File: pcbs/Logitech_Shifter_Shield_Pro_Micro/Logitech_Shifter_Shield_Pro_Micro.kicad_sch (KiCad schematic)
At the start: 12 parts, among them J1 DE9_Plug_MountingHoles, J2 AVR-ISP-6, U1 SparkFun_ProMicro

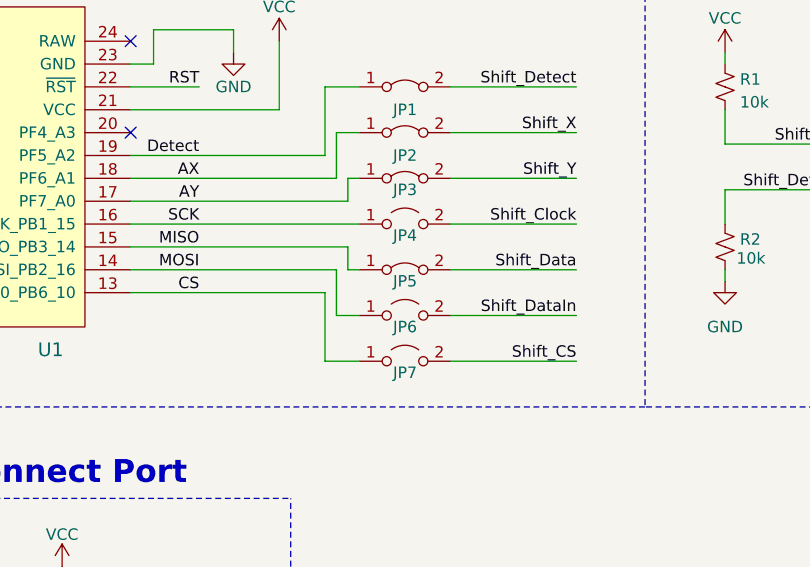
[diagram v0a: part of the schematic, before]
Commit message: Shifter: Changed all jumpers to NC
We need all of these pins in order to interface with the Logitech G25 shifter
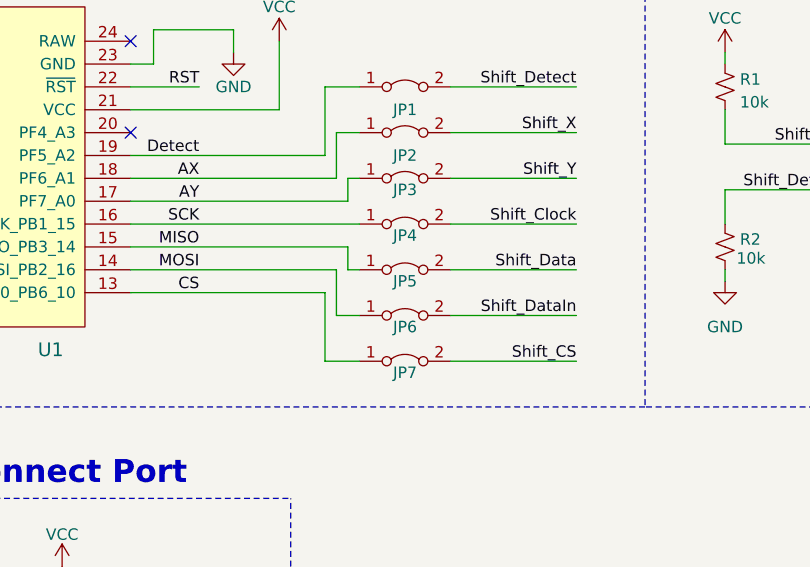
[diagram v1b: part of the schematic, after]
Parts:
- removed JP4: Clock_Jumper_NC, Jumper:SolderJumper-2_P1.3mm_Open_RoundedPad1.0x1.5mm, symbol Jumper:Jumper_2_Open
- removed JP6: Data_In_Jumper_NC, Jumper:SolderJumper-2_P1.3mm_Open_RoundedPad1.0x1.5mm, symbol Jumper:Jumper_2_Open
- removed JP7: CS_Jumper_NC, Jumper:SolderJumper-2_P1.3mm_Open_RoundedPad1.0x1.5mm, symbol Jumper:Jumper_2_Open
- added JP4: Clock_Jumper, Sim_Racing_Shields:SolderJumper-2_P1.3mm_Bridged_RoundedPad1.0x1.5mm_Unmasked, symbol Jumper:Jumper_2_Bridged
- added JP6: Data_In_Jumper, Sim_Racing_Shields:SolderJumper-2_P1.3mm_Bridged_RoundedPad1.0x1.5mm_Unmasked, symbol Jumper:Jumper_2_Bridged
- added JP7: CS_Jumper, Sim_Racing_Shields:SolderJumper-2_P1.3mm_Bridged_RoundedPad1.0x1.5mm_Unmasked, symbol Jumper:Jumper_2_Bridged
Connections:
- net CS: now also JP7.1 (A)
- net MOSI: now also JP6.1 (A)
- net SCK: now also JP4.1 (A)
- net Shift_CS: now also JP7.2 (B)
- net Shift_Clock: now also JP4.2 (B)
- net Shift_DataIn: now also JP6.2 (B)
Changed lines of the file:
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@@
+	)
+	(symbol
+		(lib_id "Jumper:Jumper_2_Bridged")
+		(at 144.78 96.52 0)
+		(unit 1)
+		(exclude_from_sim no)
+		(in_bom no)
+		(on_board yes)
+		(dnp no)
+		(property "Reference" "JP7"
+			(at 144.78 97.79 0)
+			(effects
+				(font
+					(size 1.27 1.27)
+				)
+			)
+		)
+		(property "Value" "CS_Jumper"
+			(at 144.78 94.6936 0)
+			(effects
+				(font
+					(size 1.27 1.27)
+				)
+				(hide yes)
+			)
+		)
+		(property "Footprint" "Sim_Racing_Shields:SolderJumper-2_P1.3mm_Bridged_RoundedPad1.0x1.5mm_Unmasked"
+			(at 144.78 96.52 0)
+			(effects
+				(font
+					(size 1.27 1.27)
+				)
+				(hide yes)
+			)
+		)
+		(property "Datasheet" "~"
+			(at 144.78 96.52 0)
+			(effects
+				(font
+					(size 1.27 1.27)
+				)
+				(hide yes)
+			)
+		)
+		(property "Description" ""
+			(at 144.78 96.52 0)
+			(effects
+				(font
+					(size 1.27 1.27)
+				)
+				(hide yes)
+			)
+		)
+		(property "DigiKey Part Number" ""
+			(at 144.78 96.52 0)
+			(effects
+				(font
+					(size 1.27 1.27)
+				)
+				(hide yes)
+			)
+		)
+		(property "Manufacturer" ""
+			(at 144.78 96.52 0)
+			(effects
+				(font
+					(size 1.27 1.27)
+				)
+				(hide yes)
+			)
+		)
+		(property "Part Number" ""
+			(at 144.78 96.52 0)
+			(effects
+				(font
+					(size 1.27 1.27)
+				)
+				(hide yes)
+			)
+		)
+		(pin "1"
+		)
+		(pin "2"
+		)
+		(instances
+			(project "Logitech_Shifter_Shield_Pro_Micro"
+				(path "/e63e39d7-6ac0-4ffd-8aa3-1841a4541b55"
+					(reference "JP7")
+					(unit 1)
+				)
+			)
+		)
 	)
 	(symbol
@@
 	)
 	(symbol
+		(lib_id "Jumper:Jumper_2_Bridged")
+		(at 144.78 81.28 0)
+		(unit 1)
+		(exclude_from_sim no)
+		(in_bom no)
+		(on_board yes)
+		(dnp no)
+		(property "Reference" "JP4"
+			(at 144.78 82.55 0)
+			(effects
+				(font
+					(size 1.27 1.27)
+				)
+			)
+		)
+		(property "Value" "Clock_Jumper"
+			(at 144.78 79.4536 0)
+			(effects
+				(font
+					(size 1.27 1.27)
+				)
+				(hide yes)
+			)
+		)
+		(property "Footprint" "Sim_Racing_Shields:SolderJumper-2_P1.3mm_Bridged_RoundedPad1.0x1.5mm_Unmasked"
+			(at 144.78 81.28 0)
+			(effects
+				(font
+					(size 1.27 1.27)
+				)
+				(hide yes)
+			)
+		)
+		(property "Datasheet" "~"
+			(at 144.78 81.28 0)
+			(effects
+				(font
+					(size 1.27 1.27)
+				)
+				(hide yes)
+			)
+		)
+		(property "Description" ""
+			(at 144.78 81.28 0)
+			(effects
+				(font
+					(size 1.27 1.27)
+				)
+				(hide yes)
+			)
+		)
+		(property "DigiKey Part Number" ""
+			(at 144.78 81.28 0)
+			(effects
+				(font
+					(size 1.27 1.27)
+				)
+				(hide yes)
+			)
+		)
+		(property "Manufacturer" ""
+			(at 144.78 81.28 0)
+			(effects
+				(font
+					(size 1.27 1.27)
+				)
+				(hide yes)
+			)
+		)
+		(property "Part Number" ""
+			(at 144.78 81.28 0)
+			(effects
+				(font
+					(size 1.27 1.27)
+				)
+				(hide yes)
+			)
+		)
+		(pin "1"
+		)
+		(pin "2"
+		)
+		(instances
+			(project "Logitech_Shifter_Shield_Pro_Micro"
+				(path "/e63e39d7-6ac0-4ffd-8aa3-1841a4541b55"
+					(reference "JP4")
+					(unit 1)
+				)
+			)
+		)
+	)
+	(symbol
 		(lib_id "Sim_Racing_Shields:SparkFun_ProMicro")
 		(at 93.98 80.01 0)
@@
 				(path "/e63e39d7-6ac0-4ffd-8aa3-1841a4541b55"
 					(reference "U1")
-					(unit 1)
-				)
-			)
-		)
-	)
-	(symbol
-		(lib_id "Jumper:Jumper_2_Open")
-		(at 144.78 96.52 0)
-		(unit 1)
-		(exclude_from_sim no)
-		(in_bom no)
-		(on_board yes)
-		(dnp no)
-		(property "Reference" "JP7"
-			(at 144.78 97.79 0)
-			(effects
-				(font
-					(size 1.27 1.27)
-				)
-			)
-		)
-		(property "Value" "CS_Jumper_NC"
-			(at 144.78 93.345 0)
-			(effects
-				(font
-					(size 1.27 1.27)
-				)
-				(hide yes)
-			)
-		)
-		(property "Footprint" "Jumper:SolderJumper-2_P1.3mm_Open_RoundedPad1.0x1.5mm"
-			(at 144.78 96.52 0)
-			(effects
-				(font
-					(size 1.27 1.27)
-				)
-				(hide yes)
-			)
-		)
-		(property "Datasheet" "~"
-			(at 144.78 96.52 0)
-			(effects
-				(font
-					(size 1.27 1.27)
-				)
-				(hide yes)
-			)
-		)
-		(property "Description" ""
-			(at 144.78 96.52 0)
-			(effects
-				(font
-					(size 1.27 1.27)
-				)
-				(hide yes)
-			)
-		)
-		(property "DigiKey Part Number" ""
-			(at 144.78 96.52 0)
-			(effects
-				(font
-					(size 1.27 1.27)
-				)
-				(hide yes)
-			)
-		)
-		(property "Manufacturer" ""
-			(at 144.78 96.52 0)
-			(effects
-				(font
-					(size 1.27 1.27)
-				)
-				(hide yes)
-			)
-		)
-		(property "Part Number" ""
-			(at 144.78 96.52 0)
-			(effects
-				(font
-					(size 1.27 1.27)
-				)
-				(hide yes)
-			)
-		)
-		(pin "1"
-		)
-		(pin "2"
-		)
-		(instances
-			(project ""
-				(path "/e63e39d7-6ac0-4ffd-8aa3-1841a4541b55"
-					(reference "JP7")
 					(unit 1)
 				)
@@
 	)
 	(symbol
-		(lib_id "Jumper:Jumper_2_Open")
+		(lib_id "Jumper:Jumper_2_Bridged")
 		(at 144.78 91.44 0)
 		(unit 1)
@@
 			)
 		)
-		(property "Value" "Data_In_Jumper_NC"
-			(at 144.78 88.265 0)
-			(effects
-				(font
-					(size 1.27 1.27)
-				)
-				(hide yes)
-			)
-		)
-		(property "Footprint" "Jumper:SolderJumper-2_P1.3mm_Open_RoundedPad1.0x1.5mm"
+		(property "Value" "Data_In_Jumper"
+			(at 144.78 89.6136 0)
+			(effects
+				(font
+					(size 1.27 1.27)
+				)
+				(hide yes)
+			)
+		)
+		(property "Footprint" "Sim_Racing_Shields:SolderJumper-2_P1.3mm_Bridged_RoundedPad1.0x1.5mm_Unmasked"
 			(at 144.78 91.44 0)
 			(effects
@@
 		)
 		(instances
-			(project ""
+			(project "Logitech_Shifter_Shield_Pro_Micro"
 				(path "/e63e39d7-6ac0-4ffd-8aa3-1841a4541b55"
 					(reference "JP6")
@@
 					(unit 1)
 				)
-			)
-		)
-	)
-	(symbol
-		(lib_id "Jumper:Jumper_2_Open")
-		(at 144.78 81.28 0)
-		(unit 1)
-		(exclude_from_sim no)
-		(in_bom no)
-		(on_board yes)
-		(dnp no)
-		(property "Reference" "JP4"
-			(at 144.78 82.55 0)
-			(effects
-				(font
-					(size 1.27 1.27)
-				)
-			)
-		)
-		(property "Value" "Clock_Jumper_NC"
-			(at 144.78 78.105 0)
-			(effects
-				(font
-					(size 1.27 1.27)
-				)
-				(hide yes)
-			)
-		)
-		(property "Footprint" "Jumper:SolderJumper-2_P1.3mm_Open_RoundedPad1.0x1.5mm"
-			(at 144.78 81.28 0)
-			(effects
-				(font
-					(size 1.27 1.27)
-				)
-				(hide yes)
-			)
-		)
-		(property "Datasheet" "~"
-			(at 144.78 81.28 0)
-			(effects
-				(font
-					(size 1.27 1.27)
-				)
-				(hide yes)
-			)
-		)
-		(property "Description" ""
-			(at 144.78 81.28 0)
-			(effects
-				(font
-					(size 1.27 1.27)
-				)
-				(hide yes)
-			)
-		)
-		(property "DigiKey Part Number" ""
-			(at 144.78 81.28 0)
-			(effects
-				(font
-					(size 1.27 1.27)
-				)
-				(hide yes)
-			)
-		)
-		(property "Manufacturer" ""
-			(at 144.78 81.28 0)
-			(effects
-				(font
-					(size 1.27 1.27)
-				)
-				(hide yes)
-			)
-		)
-		(property "Part Number" ""
-			(at 144.78 81.28 0)
-			(effects
-				(font
-					(size 1.27 1.27)
-				)
-				(hide yes)
-			)
-		)
-		(pin "1"
-		)
-		(pin "2"
-		)
-		(instances
-			(project ""
-				(path "/e63e39d7-6ac0-4ffd-8aa3-1841a4541b55"
-					(reference "JP4")
-					(unit 1)
-				)

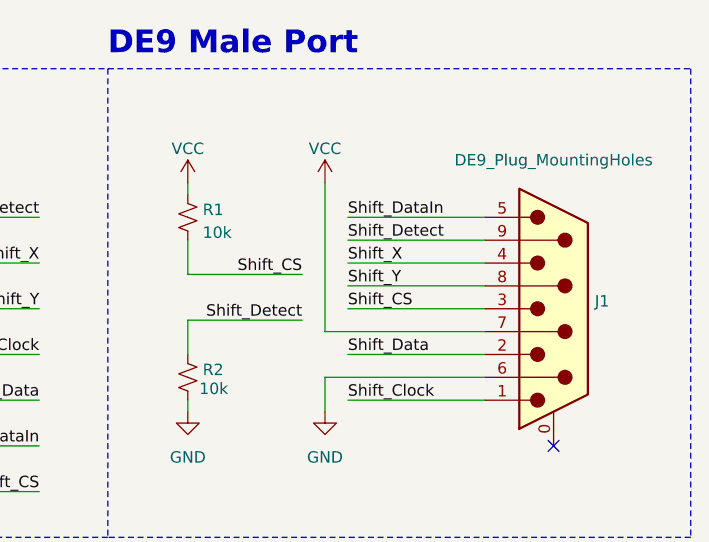
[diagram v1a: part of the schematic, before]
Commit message: Shifter: Move power to pin 9 (swap 7/9)
This is an error on the v1 PCB, and the fundamental reason why this PCB doesn't work with the G25 shifter.

On the Driving Force shifter, pins 7 and 9 are connected together internally in the DE-9 connector. Power applied to one goes to both pins, so one is used to power the shifter and the other is used with a pull-down to act as a detection pin. Since it didn't seem to matter I arbitrarily chose pin 7 as the power input for easier trace routing.

On the G25 shifter, pins *1* and 9 are connected together internally in the DE-9 connector. Pin 7 is instead attached to the clock input of the EEPROM / shift registers, and needs to be pulsed in order to get the button data from the shifter.

50/50 and I lost. Ah well.
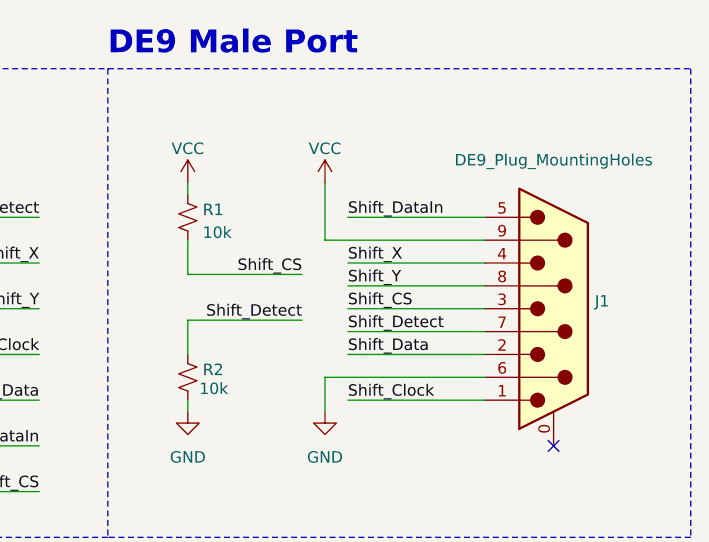
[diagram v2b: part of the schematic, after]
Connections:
- net Shift_Detect: now also J1.7; no longer J1.9
- net VCC: now also J1.9; no longer J1.7
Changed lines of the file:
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@@
 	(wire
 		(pts
-			(xy 195.58 78.74) (xy 213.36 78.74)
+			(xy 195.58 68.58) (xy 213.36 68.58)
+		)
+		(stroke
+			(width 0)
+			(type default)
+		)
+	)
+	(wire
+		(pts
+			(xy 198.12 78.74) (xy 213.36 78.74)
 		)
 		(stroke
@@
 	(wire
 		(pts
-			(xy 195.58 62.23) (xy 195.58 78.74)
+			(xy 195.58 62.23) (xy 195.58 68.58)
 		)
 		(stroke
@@
 		(pts
 			(xy 114.3 83.82) (xy 138.43 83.82)
-		)
-		(stroke
-			(width 0)
-			(type default)
-		)
-	)
-	(wire
-		(pts
-			(xy 198.12 68.58) (xy 213.36 68.58)
 		)
 		(stroke
@@
 	)
 	(label "Shift_Detect"
-		(at 198.12 68.58 0)
-		(effects
-			(font
+		(at 198.12 78.74 0)
+		(effects
+			(font

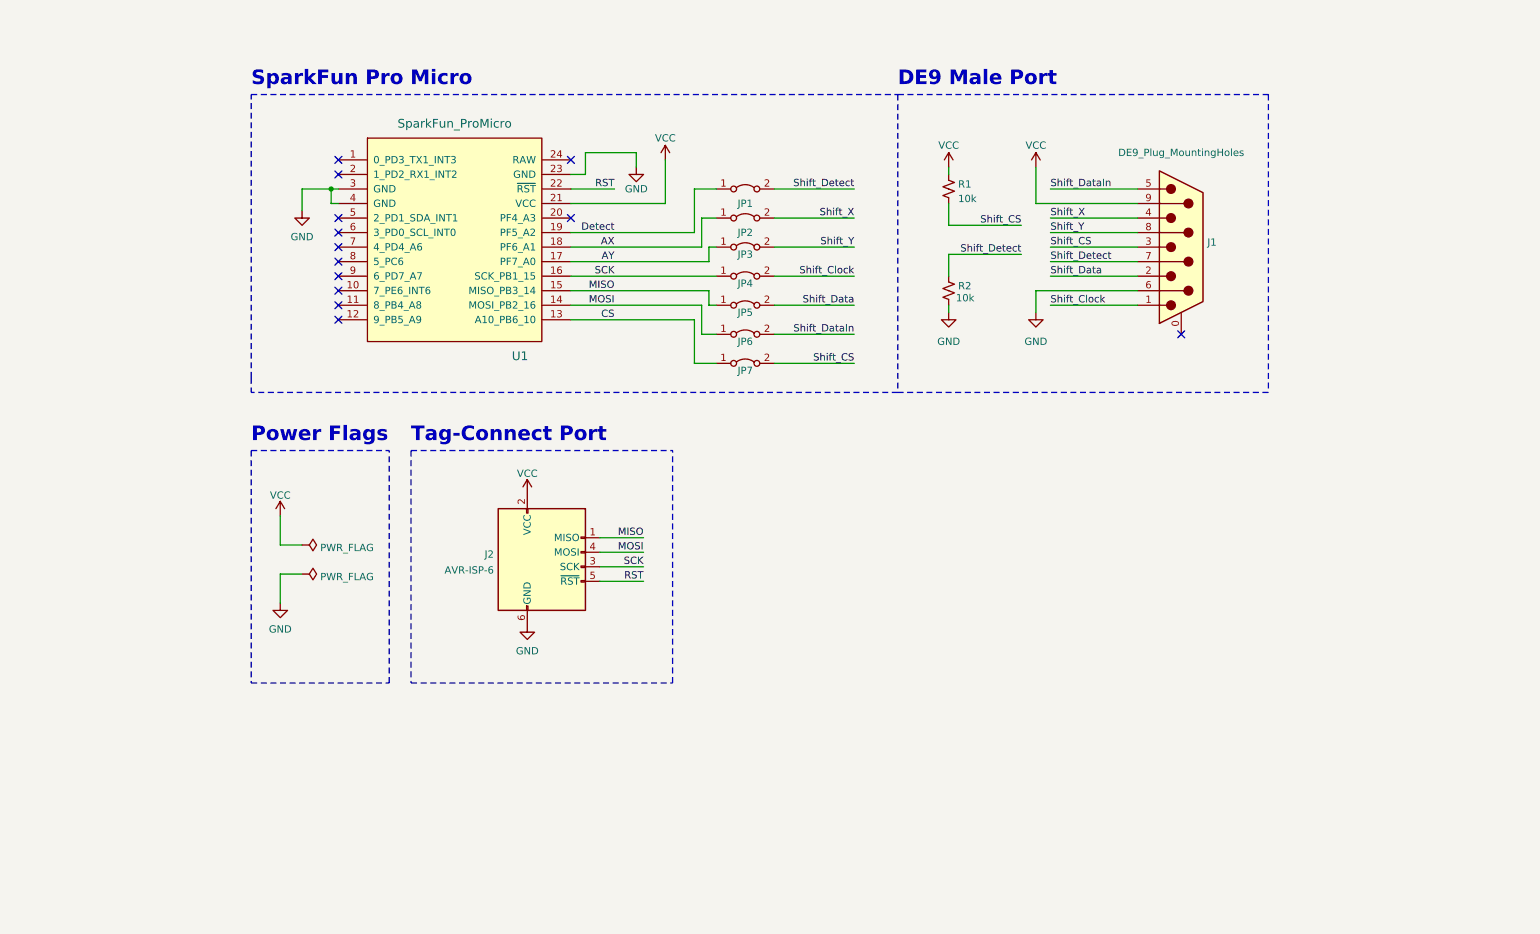
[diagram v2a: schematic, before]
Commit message: Shifter: Schematic to support G25
Adds a pull-down resistor on the second 'detect' pin, and adds three series resistors to protect against shorts between the two shifter types (Driving Force / G25).

Also renames all DE9 connections with Shift_{G25}_{G29} labels.
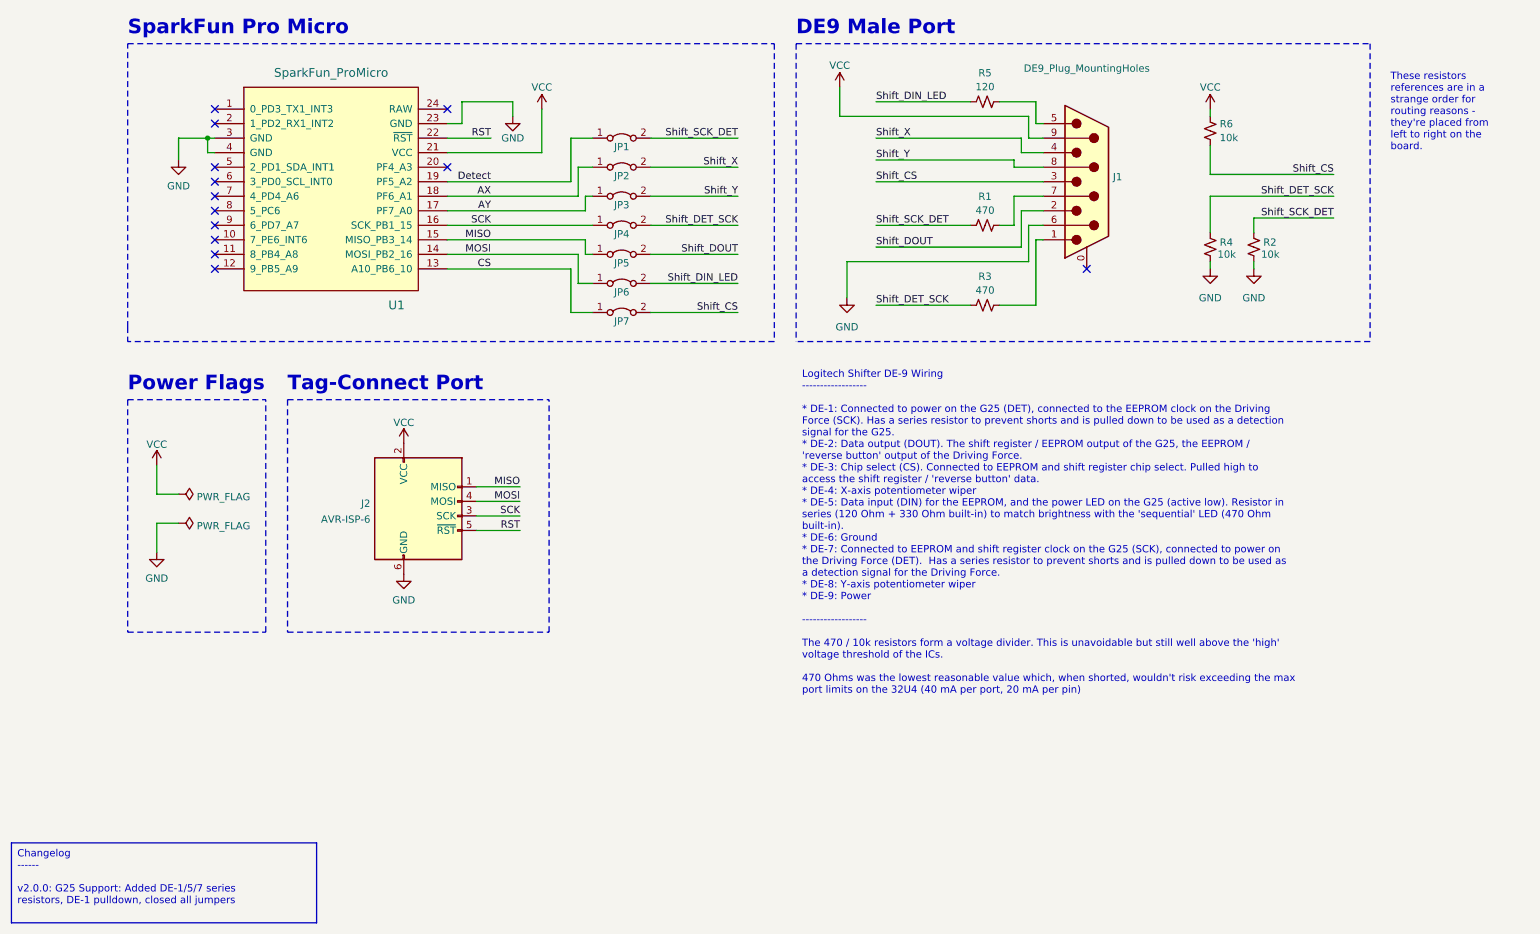
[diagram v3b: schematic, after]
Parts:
- added R1, R3: 470, Resistor_SMD:R_0805_2012Metric, symbol Device:R_Small_US
- added R2: 10k, Resistor_SMD:R_0805_2012Metric, symbol Device:R_Small_US
- added R5: 120, Resistor_SMD:R_0805_2012Metric, symbol Device:R_Small_US
- JP1: value Detect_Jumper -> SCK_DET_Jumper
- JP2: value ShiftX_Jumper -> X_Jumper
- JP3: value ShiftY_Jumper -> Y_Jumper
- JP4: value Clock_Jumper -> DET_SCK_Jumper
- JP5: value Data_Jumper -> DOUT_Jumper
- JP6: value Data_In_Jumper -> DIN_LED_Jumper
- R4: renamed from R2; DigiKey Part Number YAG1319CT-ND -> 311-10.0KCRCT-ND; Part Number RC0805FR-0710KP -> RC0805FR-0710KL
- R6: renamed from R1; DigiKey Part Number YAG1319CT-ND -> 311-10.0KCRCT-ND; Part Number RC0805FR-0710KP -> RC0805FR-0710KL
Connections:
- net GND: now also R2.1
- net Shift_Clock: no longer names the net of J1.1
- net Shift_Clock: now also R3.1; no longer JP4.2 (B)
- net Shift_Data renamed Shift_DOUT
- net Shift_DataIn: no longer names the net of J1.5
- net Shift_DataIn: now also R5.1; no longer JP6.2 (B)
- removed net Shift_Detect: J1.7, JP1.2 (B), R4.2
- new net: J1.7, R1.1
- new net Shift_DET_SCK: JP4.2 (B), R3.2, R4.2
- new net Shift_DIN_LED: JP6.2 (B), R5.2
- new net Shift_SCK_DET: JP1.2 (B), R1.2, R2.2
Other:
- moved on the sheet: J1, J2, JP1, JP2, JP3, JP4, JP5, JP6, JP7, R4, R6, U1

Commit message: Shifter: Modify PCB for G25
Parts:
- J1: footprint Connector_Dsub:DSUB-9_Male_Horizontal_P2.77x2.84mm_EdgePinOffset7.70mm_Housed_MountingHolesOffset9.12mm -> Sim_Racing_Shields:DSUB-9_Male_Horizontal_P2.77x2.84mm_EdgePinOffset7.70mm_Housed_MountingHolesOffset9.12mm_ModP1Silk
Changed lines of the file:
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@@
 			)
 		)
-		(property "Footprint" "Connector_Dsub:DSUB-9_Male_Horizontal_P2.77x2.84mm_EdgePinOffset7.70mm_Housed_MountingHolesOffset9.12mm"
+		(property "Footprint" "Sim_Racing_Shields:DSUB-9_Male_Horizontal_P2.77x2.84mm_EdgePinOffset7.70mm_Housed_MountingHolesOffset9.12mm_ModP1Silk"
 			(at 204.47 64.77 0)
 			(effects
